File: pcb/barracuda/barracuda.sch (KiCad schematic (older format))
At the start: 69 parts, among them SW1 SW_PUSH, SW10 SW_PUSH, SW11 SW_PUSH, SW12 SW_PUSH, SW13 SW_PUSH, SW14 SW_PUSH, SW15 SW_PUSH, SW16 SW_PUSH, SW17 SW_PUSH, SW18 SW_PUSH, SW19 SW_PUSH, SW2 SW_PUSH, SW20 SW_PUSH, SW21 SW_PUSH, SW22 SW_PUSH, SW23 SW_PUSH, SW24 SW_PUSH, SW25 SW_PUSH, SW26 SW_PUSH, SW27 SW_PUSH, SW28 SW_PUSH, SW29 SW_PUSH, SW3 SW_PUSH, SW30 SW_PUSH, SW31 SW_PUSH, SW32 SW_PUSH, SW33 SW_PUSH, SW4 SW_PUSH, SW5 SW_PUSH, SW6 SW_PUSH, SW7 SW_PUSH, SW8 SW_PUSH, SW9 SW_PUSH, U1 ProMicro

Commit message: PCB almost done
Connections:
- net row0: now also U1.10 (7/E6); no longer U1.7 (4/D4)
- net row1: now also U1.11 (8/B4); no longer U1.8 (5/C6)
- net row2: now also U1.12 (9/B5); no longer U1.9 (6/D7)
- net row3: now also U1.7 (4/D4); no longer U1.10 (7/E6)
- net row4: now also U1.8 (5/C6); no longer U1.11 (8/B4)
- net row5: now also U1.9 (6/D7); no longer U1.12 (9/B5)
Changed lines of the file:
@@
 	5125 5200 6000 5200
 Connection ~ 5125 5200
-Text GLabel 1300 6975 0    50   Input Italic 0
+Text GLabel 1325 7275 0    50   Input Italic 0
 row0
-Text GLabel 1300 7075 0    50   Input Italic 0
+Text GLabel 1325 7375 0    50   Input Italic 0
 row1
-Text GLabel 1300 7175 0    50   Input Italic 0
+Text GLabel 1325 7475 0    50   Input Italic 0
 row2
-Text GLabel 1300 7275 0    50   Input Italic 0
+Text GLabel 1325 6975 0    50   Input Italic 0
 row3
-Text GLabel 1300 7375 0    50   Input Italic 0
+Text GLabel 1325 7075 0    50   Input Italic 0
 row4
-Text GLabel 1300 7475 0    50   Input Italic 0
+Text GLabel 1325 7175 0    50   Input Italic 0
 row5
 Text GLabel 2925 6775 2    50   Input Italic 0
@@
 Wire Wire Line
 	2825 7275 2925 7275
-Wire Wire Line
-	1300 6975 1425 6975
-Wire Wire Line
-	1300 7075 1425 7075
-Wire Wire Line
-	1300 7175 1425 7175
-Wire Wire Line
-	1300 7375 1425 7375
-Wire Wire Line
-	1300 7475 1425 7475
-Wire Wire Line
-	1300 7275 1425 7275
 NoConn ~ 2825 6375
 NoConn ~ 2825 7475
@@
 Wire Wire Line
 	2500 5200 4250 5200
+Wire Wire Line
+	1325 7275 1425 7275
+Wire Wire Line
+	1325 7375 1425 7375
+Wire Wire Line
+	1325 7475 1425 7475
+Wire Wire Line
+	1325 6975 1425 6975
+Wire Wire Line
+	1325 7075 1425 7075
+Wire Wire Line
+	1325 7175 1425 7175
 $EndSCHEMATC

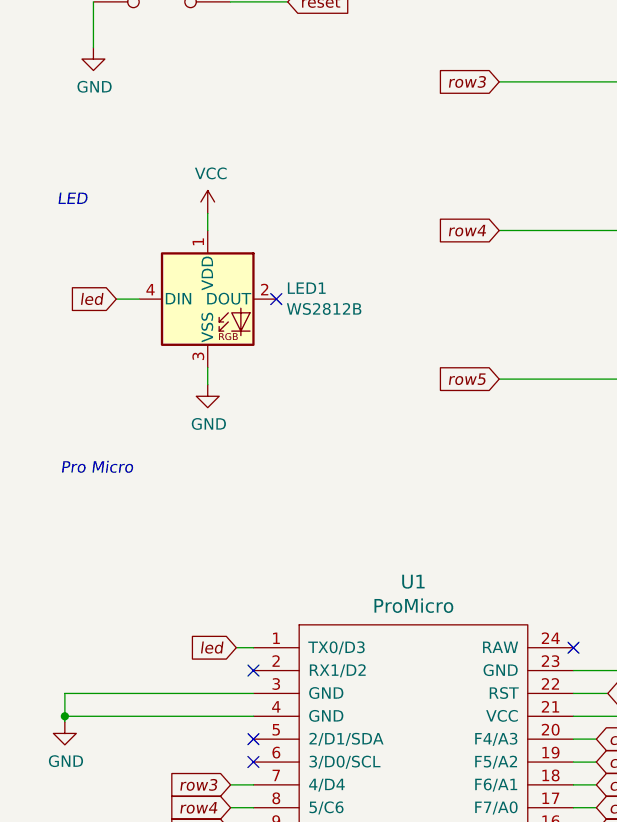
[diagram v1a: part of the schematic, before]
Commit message: Replaced KeySwitch and diode footprints
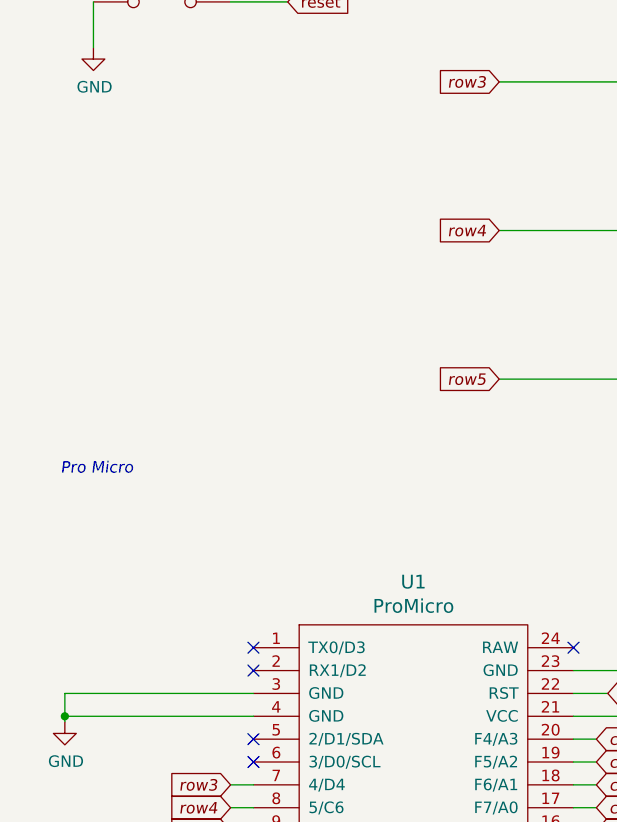
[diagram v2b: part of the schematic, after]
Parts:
- removed LED1: WS2812B, LED_SMD:LED_WS2812B_PLCC4_5.0x5.0mm_P3.2mm, symbol LED:WS2812B
- D1, D10, D11, D12, D13, D14, D15, D16, D17, D18, D19, D2, D20, D21, D22, D23, D24, D25, D26, D27, D28, D29, D3, D30, D31, D32, D33, D4, D5, D6, D7, D8, D9: footprint kbd:D3_SMD -> barracuda:D3_SMD
- SW1, SW10, SW11, SW12, SW13, SW14, SW15, SW16, SW17, SW18, SW19, SW2, SW20, SW21, SW22, SW23, SW24, SW25, SW26, SW27, SW28, SW29, SW3, SW30, SW31, SW32, SW33, SW4, SW5, SW6, SW7, SW8, SW9: footprint kbd:CherryMX_Choc_Hotswap -> kbd:ChocV1_V2_Hotswap
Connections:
- net led: no longer names the net of U1.1 (TX0/D3)
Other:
- note removed: "LED"

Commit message: Updated the MCU to atmega32u2
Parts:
- removed U1: ProMicro, Keebio-Parts:ArduinoProMicro, symbol kbd:ProMicro
- added C1, C2: 22p, Capacitor_SMD:C_0603_1608Metric_Pad1.08x0.95mm_HandSolder, symbol Device:C_Small
- added C3: 0.1u, Capacitor_SMD:C_0603_1608Metric_Pad1.08x0.95mm_HandSolder, symbol Device:C
- added C4: 10u, Capacitor_SMD:C_0805_2012Metric_Pad1.18x1.45mm_HandSolder, symbol Device:C_Small
- added C5: 1u, Capacitor_SMD:C_0603_1608Metric_Pad1.08x0.95mm_HandSolder, symbol Device:C_Small
- added C6: 0.1u, Capacitor_SMD:C_0603_1608Metric_Pad1.08x0.95mm_HandSolder, symbol Device:C_Small
- added F1: Polyfuse_Small, barracuda:RESC1206X70N, symbol Device:Polyfuse_Small
- added J1: USB_B_Micro, barracuda:HRS_ZX62R-B-5P, symbol Connector:USB_B_Micro
- added R1, R2: 22, Resistor_SMD:R_0805_2012Metric_Pad1.20x1.40mm_HandSolder, symbol Device:R
- added R3: 10k, Resistor_SMD:R_0805_2012Metric_Pad1.20x1.40mm_HandSolder, symbol Device:R
- added R4: 10k, Resistor_SMD:R_0805_2012Metric_Pad1.20x1.40mm_HandSolder, symbol Device:R_Small
- added U1: ATmega32U2-AU, Package_QFP:TQFP-32_7x7mm_P0.8mm, symbol MCU_Microchip_ATmega:ATmega32U2-AU
- added Y1: Crystal_GND24_Small, Crystal:Crystal_SMD_SeikoEpson_FA238-4Pin_3.2x2.5mm_HandSoldering, symbol Device:Crystal_GND24_Small
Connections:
- net GND: now also C1.2, C2.2, C3.2, C4.2, C5.2, C6.2, J1.5 (GND), J1.6 (Shield), R4.2, U1.28 (UGND), U1.3 (GND), Y1.2, Y1.4
- net VCC: now also C4.1, C5.1, C6.1, F1.1, R3.1, U1.31 (UVCC), U1.32 (AVCC), U1.4 (VCC)
- net col0: now also U1.14 (PB0)
- net col1: now also U1.15 (PB1)
- net col2: now also U1.16 (PB2)
- net col3: now also U1.17 (PB3)
- net col4: now also U1.18 (PB4)
- net col5: now also U1.9 (PD3)
- net reset: now also R3.2, U1.24 (PC1/~RESET)
- net row0: now also U1.26 (PC4)
- net row1: now also U1.25 (PC5)
- net row2: now also U1.23 (PC6)
- net row3: now also U1.20 (PB6)
- net row4: now also U1.21 (PB7)
- net row5: now also U1.5 (PC2)
- new net: C1.1, U1.1 (XTAL1), Y1.1
- new net: R4.1, U1.13 (~HWB~/PD7)
- new net: C2.1, U1.2 (PC0/XTAL2), Y1.3
- new net: C3.1, U1.27 (UCAP)
- new net: F1.2, J1.1 (VBUS)
- new net: J1.2 (D-), R2.2
- new net: J1.3 (D+), R1.2
- new net d_m: R2.1, U1.30 (D-)
- new net d_p: R1.1, U1.29 (D+)
- no-connect marks 7 -> 9

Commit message: save
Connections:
- net col0: now also U1.10 (PD4); no longer U1.14 (PB0)
- net col1: now also U1.11 (PD5); no longer U1.15 (PB1)
- net col2: now also U1.12 (PD6); no longer U1.16 (PB2)
- net col3: now also U1.14 (PB0); no longer U1.17 (PB3)
- net col4: now also U1.15 (PB1); no longer U1.18 (PB4)
- net col5: now also U1.16 (PB2); no longer U1.9 (PD3)
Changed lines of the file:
@@
 Text GLabel 10950 4250 2    50   Input Italic 0
 row5
+Text GLabel 10950 5250 2    50   Input Italic 0
+col0
+Text GLabel 10950 5350 2    50   Input Italic 0
+col1
+Text GLabel 10950 5450 2    50   Input Italic 0
+col2
 Text GLabel 10950 3350 2    50   Input Italic 0
-col0
+col3
 Text GLabel 10950 3450 2    50   Input Italic 0
-col1
+col4
 Text GLabel 10950 3550 2    50   Input Italic 0
-col2
-Text GLabel 10950 3650 2    50   Input Italic 0
-col3
-Text GLabel 10950 3750 2    50   Input Italic 0
-col4
-Text GLabel 10950 5150 2    50   Input Italic 0
 col5
 Connection ~ 3350 1575
@@
 Connection ~ 10150 3050
 Wire Wire Line
-	10850 3350 10950 3350
-Wire Wire Line
-	10850 3450 10950 3450
-Wire Wire Line
-	10850 3550 10950 3550
-Wire Wire Line
-	10850 3650 10950 3650
-Wire Wire Line
-	10850 3750 10950 3750
-Wire Wire Line
 	10850 3950 10950 3950
 Wire Wire Line
@@
 NoConn ~ 10850 4950
 NoConn ~ 10850 5050
-NoConn ~ 10850 5250
-NoConn ~ 10850 5350
-NoConn ~ 10850 5450
 $Comp
 L Connector:USB_B_Micro J1
@@
 Wire Wire Line
 	950  6600 950  6800
-Wire Wire Line
-	10850 5150 10950 5150
 NoConn ~ 10850 3850
 $Comp
@@
 Wire Wire Line
 	10925 5825 10925 5875
+Wire Wire Line
+	10850 3550 10950 3550
+Wire Wire Line
+	10850 3450 10950 3450
+Wire Wire Line
+	10850 3350 10950 3350
+Wire Wire Line
+	10850 5450 10950 5450
+Wire Wire Line
+	10850 5250 10950 5250
+Wire Wire Line
+	10850 5350 10950 5350
+NoConn ~ 10850 3650
+NoConn ~ 10850 3750
+NoConn ~ 10850 5150
 $EndSCHEMATC

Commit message: Finished routing
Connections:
- net row3: now also U1.7 (PD1); no longer U1.20 (PB6)
- net row4: now also U1.8 (PD2); no longer U1.21 (PB7)
- net row5: now also U1.9 (PD3); no longer U1.5 (PC2)
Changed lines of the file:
@@
 Text GLabel 10950 4550 2    50   Input Italic 0
 row2
-Text GLabel 10950 3950 2    50   Input Italic 0
+Text GLabel 10950 4950 2    50   Input Italic 0
 row3
-Text GLabel 10950 4050 2    50   Input Italic 0
+Text GLabel 10950 5050 2    50   Input Italic 0
 row4
-Text GLabel 10950 4250 2    50   Input Italic 0
+Text GLabel 10950 5150 2    50   Input Italic 0
 row5
 Text GLabel 10950 5250 2    50   Input Italic 0
@@
 Connection ~ 10150 3050
 Wire Wire Line
-	10850 3950 10950 3950
-Wire Wire Line
-	10850 4050 10950 4050
-Wire Wire Line
-	10850 4250 10950 4250
-Wire Wire Line
 	10850 4350 10950 4350
 Wire Wire Line
@@
 NoConn ~ 10850 4650
 NoConn ~ 10850 4850
-NoConn ~ 10850 4950
-NoConn ~ 10850 5050
 $Comp
 L Connector:USB_B_Micro J1
@@
 NoConn ~ 10850 3650
 NoConn ~ 10850 3750
-NoConn ~ 10850 5150
+Wire Wire Line
+	10850 4950 10950 4950
+Wire Wire Line
+	10850 5050 10950 5050
+Wire Wire Line
+	10850 5150 10950 5150
+NoConn ~ 10850 3950
+NoConn ~ 10850 4050
+NoConn ~ 10850 4250
 $EndSCHEMATC
